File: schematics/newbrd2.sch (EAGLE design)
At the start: 36 parts, among them U1 ADXL375BCCZ, U2 AD5241BRU1M-REEL7AD5241BRZ1M

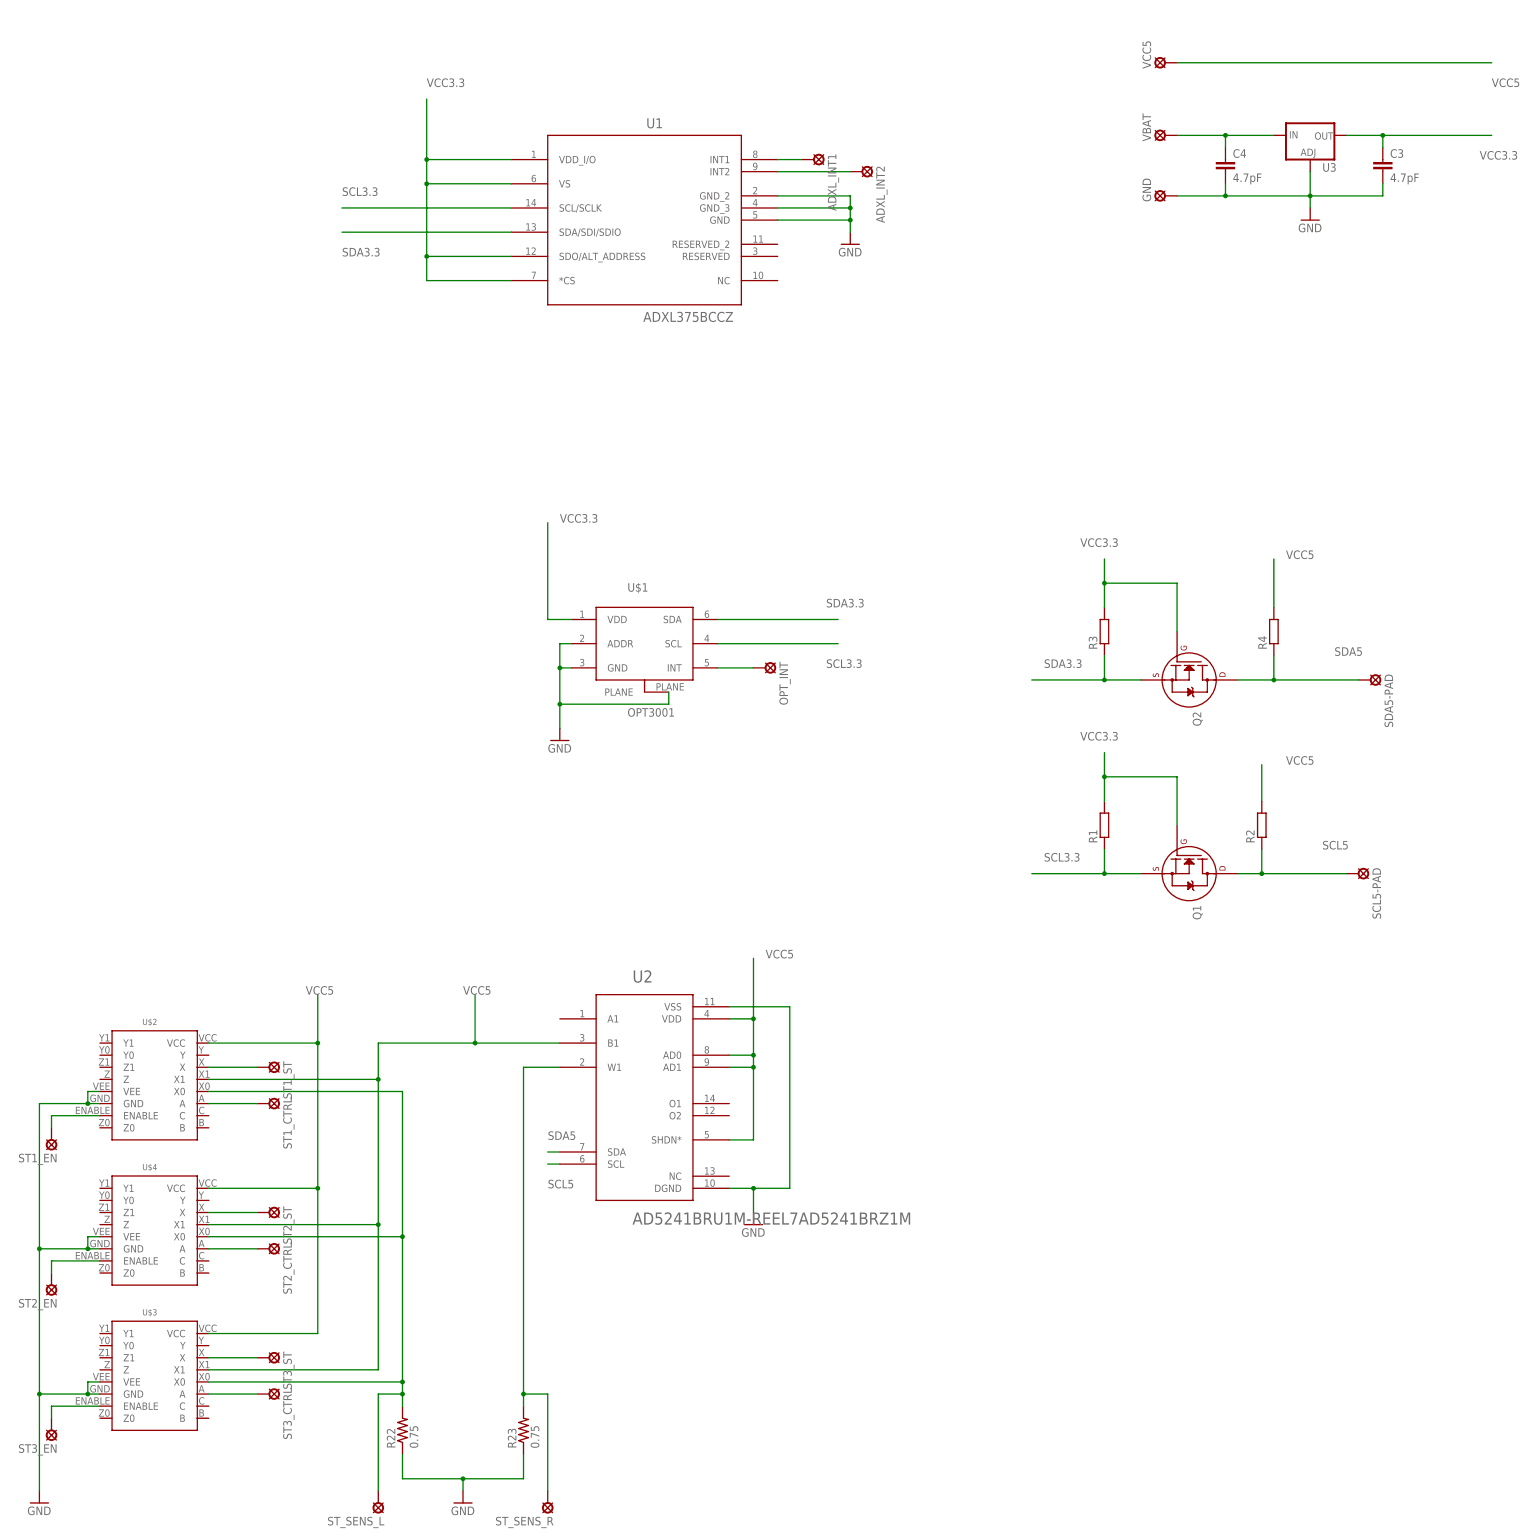
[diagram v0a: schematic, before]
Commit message: Правки платы для аналоговых устройств и доделана плата для I2C устройств
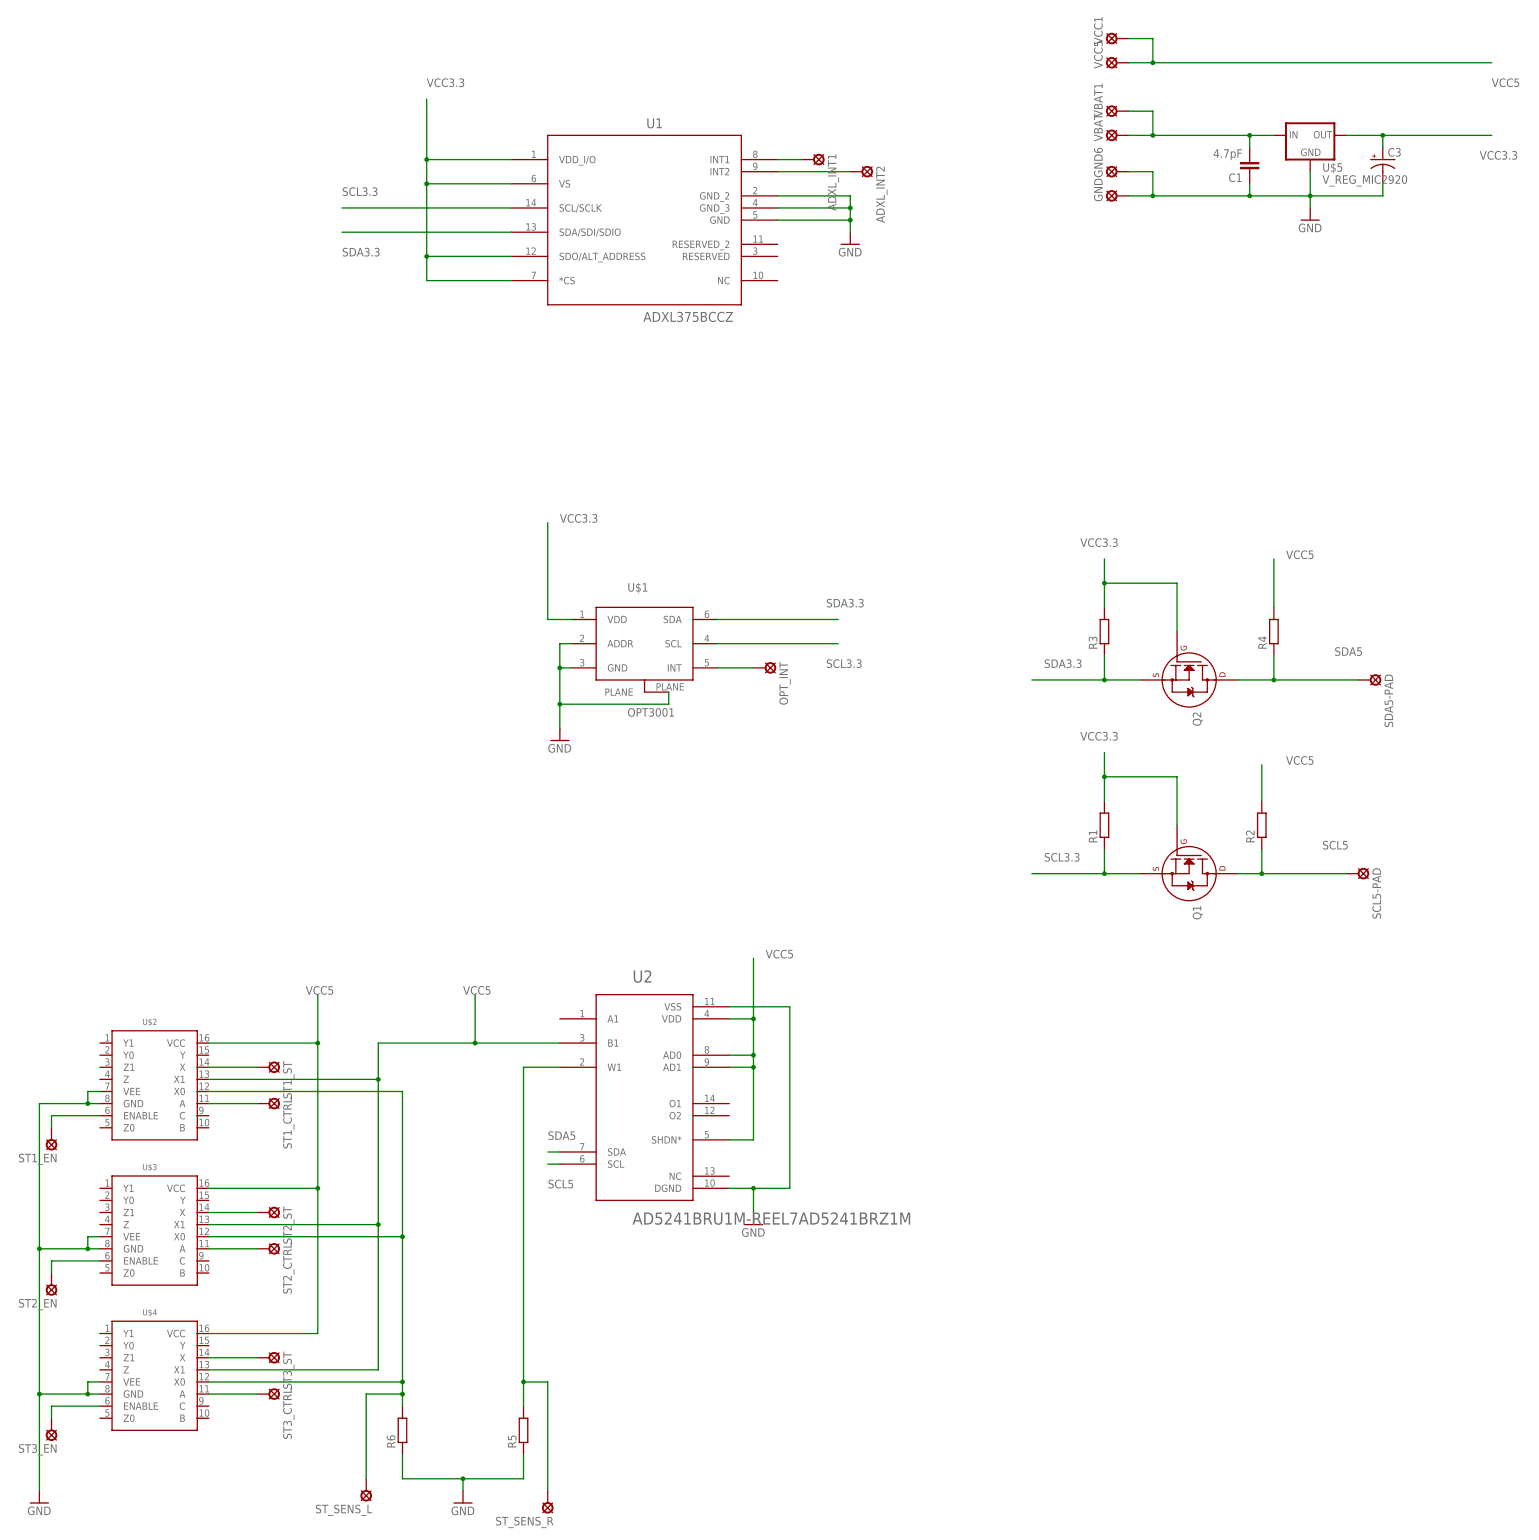
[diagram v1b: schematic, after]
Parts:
- removed C4: 4.7pF, SparkFun-Capacitors:4.7PF-50V(-/+.25PF)(0603)
- removed R22, R23: 0.75, SparkFun-Resistors:0.75OHM-1/4W-1%(0805)
- removed U3: (no value), elements:LD1117S50
- added C1: 4.7pF, rcl:C-EUC0603
- added GND6, VBAT1, VCC1: LSP10, solpad:LSP10
- added R5, R6: (no value), resistor:R-EU_R0805
- added U$5: V_REG_MIC2920, SparkFun-PowerIC:V_REG_MIC2920
- C3: value 4.7pF -> (none); device SparkFun-Capacitors:4.7PF-50V(-/+.25PF)(0603) -> SparkFun-Capacitors:CAP_POL3528
- U$2, U$3, U$4: value MC74HC4051A -> MC74HC4051AMC74HC4051AG; device elements:MC74HC4051A -> elements:MC74HC4051AMC74HC4051AG
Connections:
- net GND: now also C1.1, C3.-, GND6.MP, R5.1, R6.1, U$5.GND; no longer C3.2, C4.2, R22.1, R23.1, U3.ADJ
- net N$1: now also C1.2, U$5.IN, VBAT1.MP; no longer C4.1, U3.IN
- net N$11: now also U$3.ENABLE; no longer U$4.ENABLE
- net N$12: now also U$3.A; no longer U$4.A
- net N$13: now also U$4.A; no longer U$3.A
- net N$4: now also U$4.ENABLE; no longer U$3.ENABLE
- net N$5: now also U$3.X; no longer U$4.X
- net N$6: now also U$4.X; no longer U$3.X
- net N$8: now also R5.2, U2.W1; no longer R23.2
- net N$9: now also R6.2; no longer R22.2
- net VCC3.3: now also C3.+, U$5.OUT; no longer C3.1, U3.OUT
- net VCC5: now also U2.B1, VCC1.MP
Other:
- moved on the sheet: GND, ST_SENS_L, U$2, U$3, U$4, VBAT, VCC5
